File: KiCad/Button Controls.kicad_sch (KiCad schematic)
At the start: 8 parts, among them J3 691137710003, J4 691137710002, SW1 SW_Push_Dual, SW2 SW_Push_Dual, SW3 SW_Push_Dual

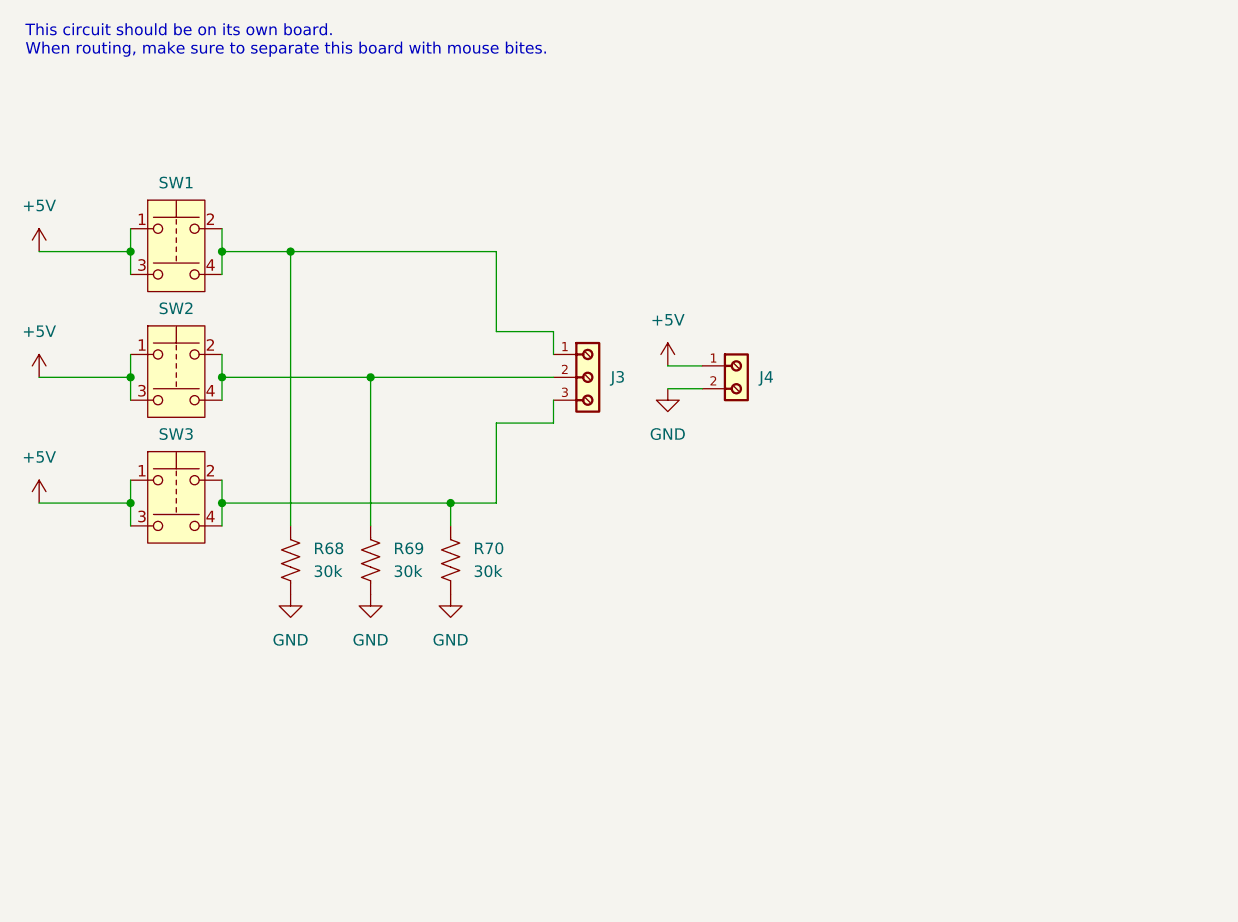
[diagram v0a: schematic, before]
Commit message: corrected push button's symbol on schematic
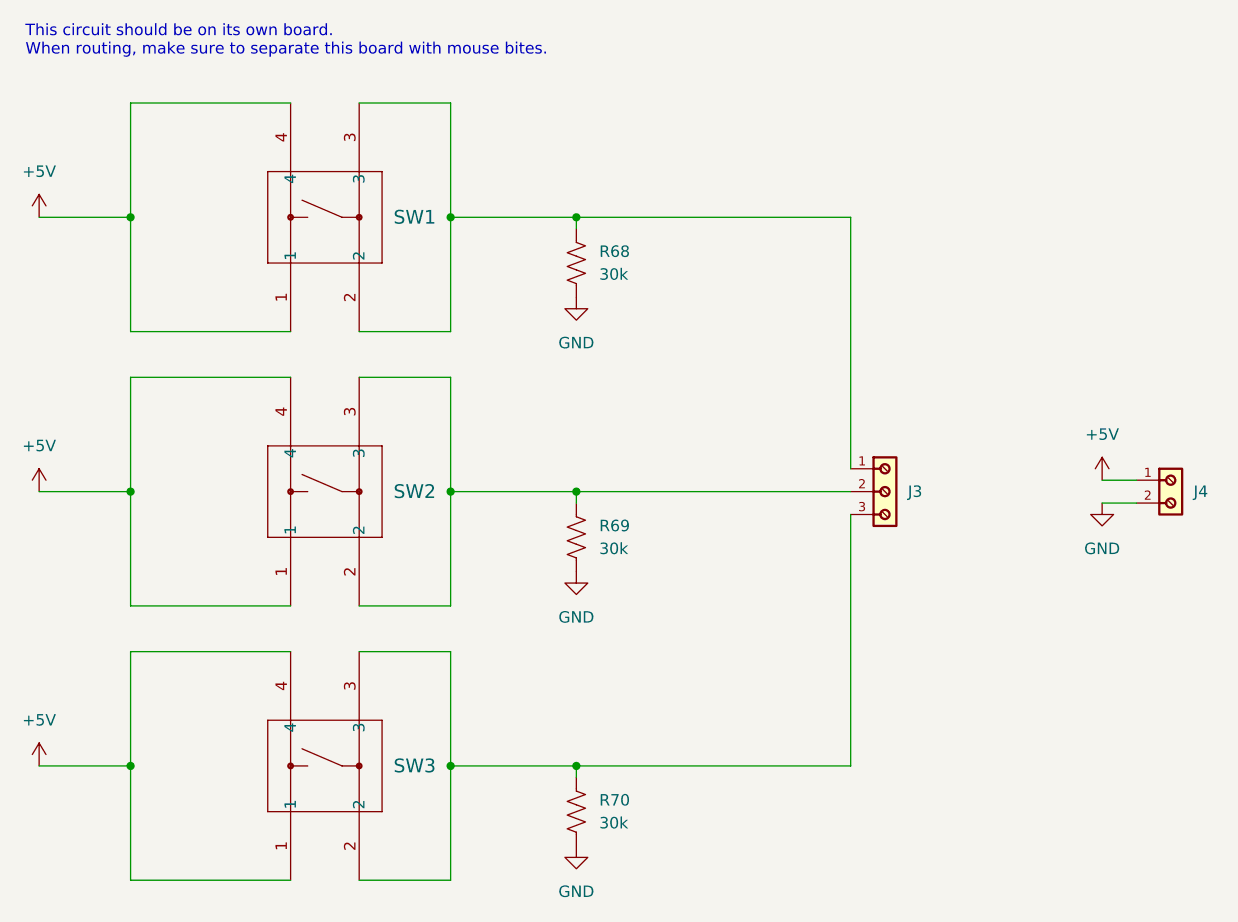
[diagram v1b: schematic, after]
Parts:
- removed SW1, SW2, SW3: SW_Push_Dual, Switch Push Button D6R90F2LFS:D6R90_CNK, symbol Switch:SW_Push_Dual
- added SW1, SW2, SW3: D6R90F2LFS, Switch Push Button D6R90F2LFS:D6R90_CNK, symbol Switch Push Button D6R90F2LFS:D6R90F2LFS
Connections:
- net +5V: now also SW1.1, SW1.4, SW2.1, SW2.4, SW3.1, SW3.4
- net at J3.2, R69.1: now also SW2.2, SW2.3
- net at J3.1, R68.1: now also SW1.2, SW1.3
- net at J3.3, R70.1: now also SW3.2, SW3.3

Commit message: routed the filter, updated 0201 footprints to 0402
JLCPCB's economy PCBA has a footprint bottom limit of 0402 imperial
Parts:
- R68, R69, R70: footprint Resistor_SMD:R_0201_0603Metric -> Resistor_SMD:R_0402_1005Metric
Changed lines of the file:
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@@
 			)
 		)
-		(property "Footprint" "Resistor_SMD:R_0201_0603Metric"
+		(property "Footprint" "Resistor_SMD:R_0402_1005Metric"
 			(at 86.106 122.174 90)
 			(hide yes)
@@
 			)
 		)
-		(property "Footprint" "Resistor_SMD:R_0201_0603Metric"
+		(property "Footprint" "Resistor_SMD:R_0402_1005Metric"
 			(at 86.106 91.694 90)
 			(hide yes)
@@
 			)
 		)
-		(property "Footprint" "Resistor_SMD:R_0201_0603Metric"
+		(property "Footprint" "Resistor_SMD:R_0402_1005Metric"
 			(at 86.106 61.214 90)
 			(hide yes)

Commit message: all SMD are 0603 (imperial) now, started rerouting all traces
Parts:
- R68, R69, R70: footprint Resistor_SMD:R_0402_1005Metric -> Resistor_SMD:R_0603_1608Metric
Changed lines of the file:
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@@
+			)
+		)
+		(property "LCSC Part #" ""
+			(at 152.4 87.63 90)
+			(hide yes)
+			(show_name no)
+			(do_not_autoplace no)
+			(effects
+				(font
+					(size 1.27 1.27)
+				)
 			)
 		)
@@
 			)
 		)
-		(property "Footprint" "Resistor_SMD:R_0402_1005Metric"
+		(property "Footprint" "Resistor_SMD:R_0603_1608Metric"
 			(at 86.106 122.174 90)
 			(hide yes)
@@
 			)
 		)
+		(property "LCSC Part #" ""
+			(at 85.09 121.92 0)
+			(hide yes)
+			(show_name no)
+			(do_not_autoplace no)
+			(effects
+				(font
+					(size 1.27 1.27)
+				)
+			)
+		)
 		(pin "1"
 		)
@@
 			)
 		)
-		(property "Footprint" "Resistor_SMD:R_0402_1005Metric"
+		(property "Footprint" "Resistor_SMD:R_0603_1608Metric"
 			(at 86.106 91.694 90)
 			(hide yes)
@@
 			)
 		)
+		(property "LCSC Part #" ""
+			(at 85.09 91.44 0)
+			(hide yes)
+			(show_name no)
+			(do_not_autoplace no)
+			(effects
+				(font
+					(size 1.27 1.27)
+				)
+			)
+		)
 		(pin "1"
 		)
@@
 			)
 		)
+		(property "LCSC Part #" ""
+			(at 53.34 99.06 90)
+			(hide yes)
+			(show_name no)
+			(do_not_autoplace no)
+			(effects
+				(font
+					(size 1.27 1.27)
+				)
+			)
+		)
 		(pin "4"
 		)
@@
 			)
 		)
-		(property "Footprint" "Resistor_SMD:R_0402_1005Metric"
+		(property "Footprint" "Resistor_SMD:R_0603_1608Metric"
 			(at 86.106 61.214 90)
 			(hide yes)
@@
 			)
 		)
+		(property "LCSC Part #" ""
+			(at 85.09 60.96 0)
+			(hide yes)
+			(show_name no)
+			(do_not_autoplace no)
+			(effects
+				(font
+					(size 1.27 1.27)
+				)
+			)
+		)
 		(pin "1"
 		)
@@
 			)
 		)
+		(property "LCSC Part #" ""
+			(at 53.34 68.58 90)
+			(hide yes)
+			(show_name no)
+			(do_not_autoplace no)
+			(effects
+				(font
+					(size 1.27 1.27)
+				)
+			)
+		)
 		(pin "4"
 		)
@@
 			)
 		)
+		(property "LCSC Part #" ""
+			(at 53.34 129.54 90)
+			(hide yes)
+			(show_name no)
+			(do_not_autoplace no)
+			(effects
+				(font
+					(size 1.27 1.27)
+				)
+			)
+		)
 		(pin "4"
 		)
@@
 			(hide yes)
 			(show_name no)
+			(do_not_autoplace no)
+			(effects
+				(font
+					(size 1.27 1.27)
+				)
+			)
+		)
+		(property "LCSC Part #" ""
+			(at 120.65 86.36 90)
+			(hide yes)
+			(show_name no)
